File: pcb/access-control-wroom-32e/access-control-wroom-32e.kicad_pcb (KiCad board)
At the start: 2 copper layers, 71.3 x 63.3 mm, 31 parts, among them J1 CON_I2C, K1 G5LE-1, U1 ESP32-DevKitC

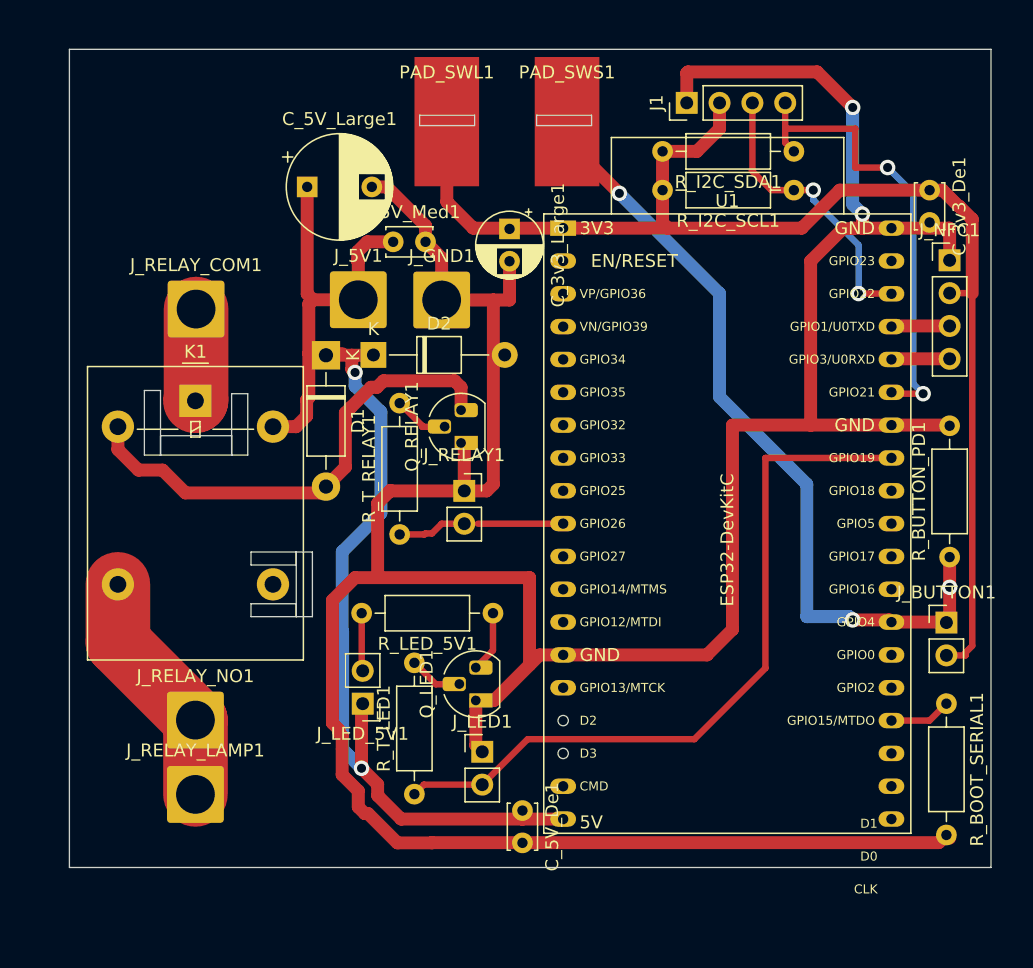
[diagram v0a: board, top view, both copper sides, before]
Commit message: Refined access controll dev box
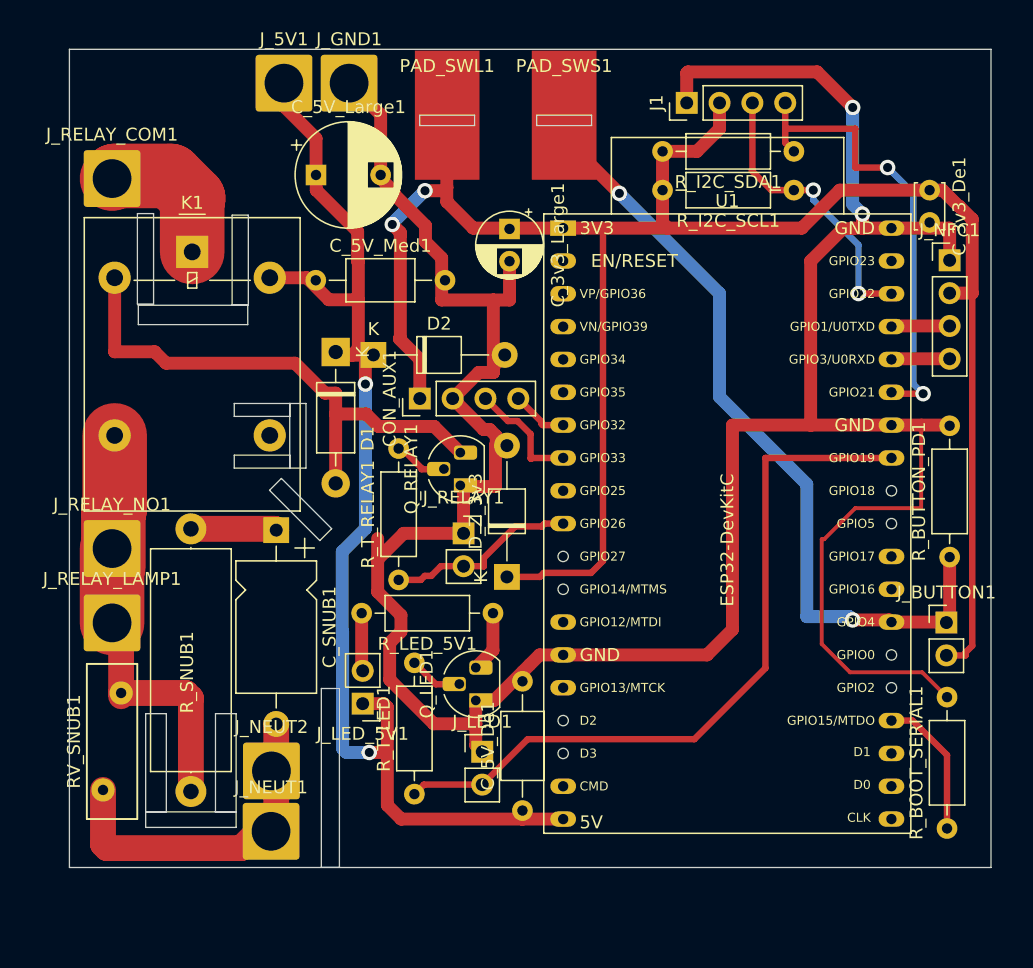
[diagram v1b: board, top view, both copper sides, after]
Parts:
- added CON_AUX1: Conn_01x04_Socket, Connector_PinHeader_2.54mm:PinHeader_1x04_P2.54mm_Vertical, F.Cu at (26.5, 27.0)
- added C_SNUB1: C, Capacitor_THT:CP_Axial_L10.0mm_D6.0mm_P15.00mm_Horizontal, F.Cu at (15.4, 37.2)
- added D_Z_3v3: D_Zener, Diode_THT:D_T-1_P10.16mm_Horizontal, F.Cu at (33.2, 40.8)
- added J_NEUT1: Conn_01x01_Socket, Connector_Wire:SolderWire-2.5sqmm_1x01_D2.4mm_OD4.4mm, F.Cu at (15.0, 60.5)
- added J_NEUT2: Conn_01x01_Socket, Connector_Wire:SolderWire-2.5sqmm_1x01_D2.4mm_OD4.4mm, F.Cu at (15.0, 55.8)
- added RV_SNUB1: Varistor, Varistor:RV_Disc_D12mm_W3.9mm_P7.5mm, F.Cu at (3.40, 49.8)
- added R_SNUB1: R, Resistor_THT:R_Axial_DIN0617_L17.0mm_D6.0mm_P20.32mm_Horizontal, F.Cu at (8.80, 57.4)
- C_5V_De1, C_5V_Med1: footprint Capacitor_THT:C_Disc_D3.4mm_W2.1mm_P2.50mm -> Capacitor_THT:C_Axial_L5.1mm_D3.1mm_P10.00mm_Horizontal
- R_T_LED1, R_T_RELAY1: value R -> 560R
- moved J_GND1 18.2 mm to (21.0, 2.62)
- moved J_5V1 17.7 mm to (16.0, 2.62)
- moved J_RELAY_LAMP1 14.8 mm to (2.70, 44.4)
- moved J_RELAY_NO1 14.8 mm to (2.70, 38.6)
- moved J_RELAY_COM1 12.0 mm to (2.70, 10.0)
- moved K1 11.5 mm to (8.90, 15.7)
- moved R_BOOT_SERIAL1 9.66 mm to (67.3, 60.3), turned to 90 degrees
- moved C_5V_Med1 6.69 mm to (18.5, 17.9)
- moved R_T_RELAY1 3.52 mm to (24.9, 41.0)
- moved J_RELAY1 3.29 mm to (29.9, 37.5)
- moved Q_RELAY1 3.29 mm to (29.6, 33.7)
- moved C_5V_Large1 1.15 mm to (18.5, 9.72)
- moved D1 0.79 mm to (20.0, 23.4)
- moved PAD_SWS1 0.54 mm to (37.7, 5.10)
- moved PAD_SWL1 0.50 mm to (28.6, 5.10)
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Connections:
- U1 pad 11: unconnected-(U1-ADC2_CH7/GPIO27-Pad11) -> (no net)
- U1 pad 12: unconnected-(U1-MTMS/GPIO14/ADC2_CH6-Pad12) -> (no net)
- U1 pad 7: unconnected-(U1-32K_XP/GPIO32/ADC1_CH4-Pad7) -> Net-(CON_AUX1-Pin_4)
- U1 pad 8: unconnected-(U1-32K_XN/GPIO33/ADC1_CH5-Pad8) -> Net-(CON_AUX1-Pin_3)
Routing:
- net +3V3: track 100.3 -> 153.8 mm, vias 0 -> 2
- net NEUT: track 0.00 -> 25.0 mm
- net GND: track 252.1 -> 229.8 mm
- net Net-(J_RELAY_LAMP1-Pin_1): track 18.7 -> 36.5 mm
- net Net-(CON_AUX1-Pin_3): track 0.00 -> 9.06 mm
- net Net-(C_SNUB1-Pad1): track 0.00 -> 6.78 mm
- net Net-(U1-MTDO/GPIO15/ADC2_CH3): track 4.79 -> 11.1 mm
- net Net-(CON_AUX1-Pin_4): track 0.00 -> 4.41 mm
- net Net-(J_RELAY_COM1-Pin_1): track 7.12 -> 11.2 mm
- net Net-(D1-A): track 38.0 -> 42.0 mm
- net +5V: track 95.8 -> 92.1 mm
- net Net-(J_RELAY1-Pin_2): track 11.9 -> 14.9 mm
- net Net-(J_BUTTON1-Pin_1): vias 3 -> 2
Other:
- outline, holes or cut-outs redrawn

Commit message: Updates with AUX
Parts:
- added CON_AUX2: Conn_01x04_Socket, Connector_PinHeader_2.54mm:PinHeader_1x04_P2.54mm_Vertical, F.Cu at (54.0, 62.1)
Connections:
- U1 pad : (no net) -> Net-(CON_AUX2-Pin_3)
- U1 pad 27: unconnected-(U1-GPIO16-Pad27) -> (no net)
- U1 pad 28: unconnected-(U1-GPIO17-Pad28) -> (no net)
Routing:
- net Net-(CON_AUX2-Pin_4): track 0.00 -> 35.3 mm
- net Net-(CON_AUX2-Pin_3): track 0.00 -> 32.0 mm
- net +3V3: track 153.8 -> 185.0 mm
- net GND: track 229.8 -> 247.5 mm
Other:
- board size 71.3 x 63.3 mm -> 71.4 x 63.3 mm

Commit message: Further optimisation
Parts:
- added CON_SENSE1: Conn_01x04_Socket, Connector_PinHeader_2.54mm:PinHeader_1x04_P2.54mm_Vertical, F.Cu at (33.1, 63.7)
- moved RV_SNUB1 2.29 mm to (3.38, 52.1)
- moved C_SNUB1 2.29 mm to (15.4, 39.5)
- moved J_NEUT1 2.29 mm to (15.0, 62.8)
- moved J_NEUT2 2.29 mm to (15.0, 58.1)
- moved J_RELAY_COM1 2.29 mm to (2.68, 12.3)
- moved J_RELAY_LAMP1 2.29 mm to (2.68, 46.7)
- moved J_RELAY_NO1 2.29 mm to (2.68, 40.9)
- moved K1 2.29 mm to (8.88, 18.0)
- moved R_SNUB1 2.29 mm to (8.78, 59.7)
- moved CON_AUX2 1.57 mm to (54.0, 63.7)
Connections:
- U1 pad : Net-(CON_AUX2-Pin_3) -> (no net)
- U1 pad 13: unconnected-(U1-MTDI/GPIO12/ADC2_CH5-Pad13) -> Net-(CON_SENSE1-Pin_3)
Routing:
- net +3V3: track 185.0 -> 217.5 mm, vias 2 -> 4
- net Net-(CON_SENSE1-Pin_3): track 0.00 -> 28.6 mm, vias 0 -> 2
- net +5V: track 92.1 -> 107.9 mm
- net GND: track 247.5 -> 258.7 mm, vias 2 -> 4
- net Net-(D1-A): track 42.0 -> 39.6 mm
- net Net-(CON_AUX2-Pin_3): track 32.0 -> 32.6 mm
- net Net-(CON_AUX2-Pin_4): track 35.3 -> 35.9 mm
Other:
- board size 71.4 x 63.3 mm -> 71.4 x 65.5 mm
